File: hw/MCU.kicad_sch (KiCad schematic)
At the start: 15 parts, among them J2 Conn_01x06, SW2 SKRPACE010, SW3 SKRPACE010, U2 N32L406RBL7

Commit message: updated Sheet and Board Information
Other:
- company: Qingdao IotPi Information Technology Ltd., -> Beijing Exponential Deep Space
- title: KiCad 2023 Shen Zhen Badge -> KiCad 2023 Asia Badge
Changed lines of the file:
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@@
   (paper "A4")
   (title_block
-    (title "KiCad 2023 Shen Zhen Badge")
-    (date "2023-10-04")
+    (title "KiCad 2023 Asia Badge")
+    (date "2023-10-07")
     (rev "2")
-    (company "Qingdao IotPi Information Technology Ltd.,")
+    (company "Beijing Exponential Deep Space")
     (comment 1 "Designed by Yang Hongbo")
   )

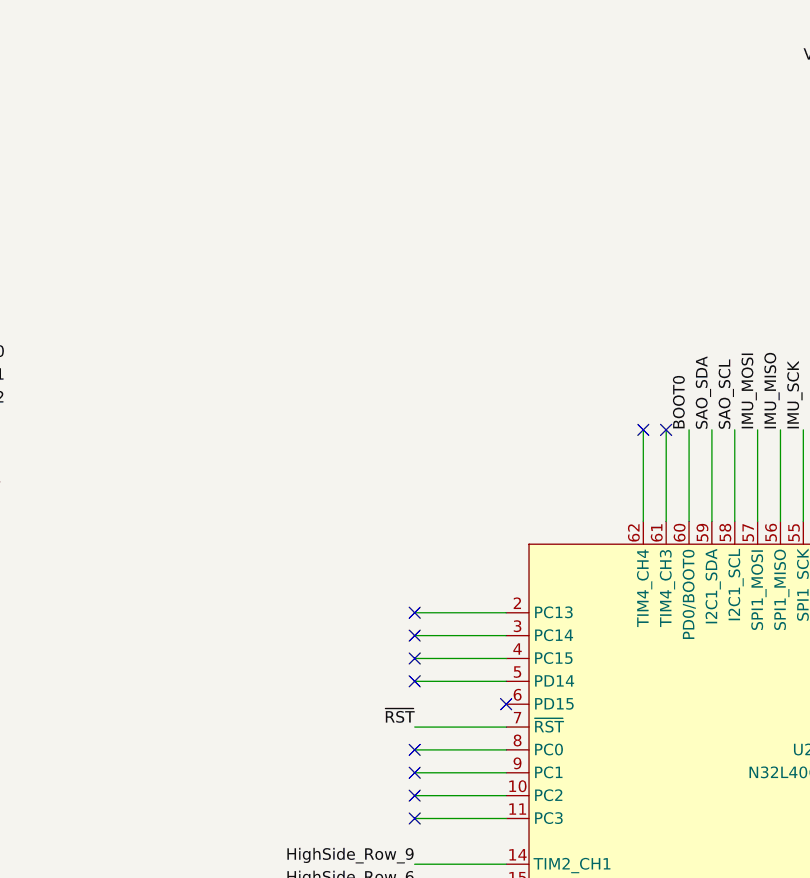
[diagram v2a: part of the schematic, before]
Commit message: added 8Mhz crystal
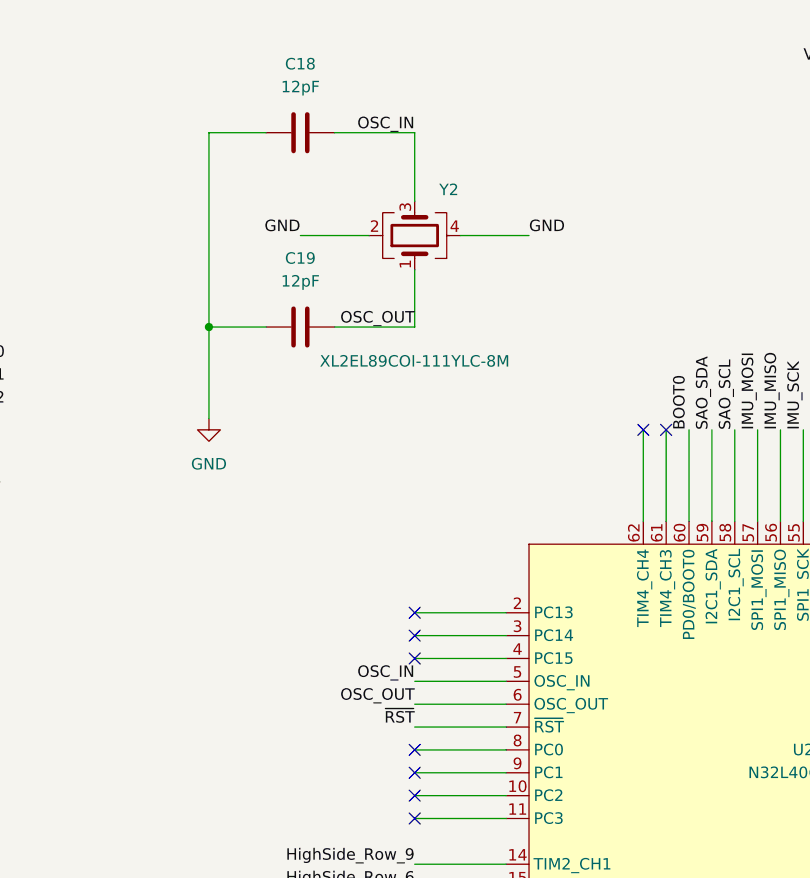
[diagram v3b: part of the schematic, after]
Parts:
- added C18, C19: 12pF, Capacitor_SMD:C_0402_1005Metric, symbol Device:C
- added Y2: XL2EL89COI-111YLC-8M, Crystal:Crystal_SMD_3225-4Pin_3.2x2.5mm, symbol Device:Crystal_GND24
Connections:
- net GND: now also C18.1, C19.1, Y2.2, Y2.4
- net OSC_IN: now reaches U2.5 (PD14)
- net OSC_IN: now also C18.2, Y2.3
- net OSC_OUT: now reaches U2.6 (PD15)
- net OSC_OUT: now also C19.2, Y2.1
- no-connect marks 18 -> 16
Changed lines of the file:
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@@
   (junction (at 114.3 172.72) (diameter 0) (color 0 0 0 0)
   )
+  (junction (at 91.44 49.53) (diameter 0) (color 0 0 0 0)
+  )
   (junction (at 264.16 142.24) (diameter 0) (color 0 0 0 0)
   )
@@
   (no_connect (at 209.55 137.16))
   (no_connect (at 114.3 96.52))
-  (no_connect (at 114.3 88.9))
   (no_connect (at 165.1 60.96))
   (no_connect (at 160.02 60.96))
   (no_connect (at 114.3 81.28))
-  (no_connect (at 124.46 91.44))
   (no_connect (at 114.3 104.14))
   (no_connect (at 114.3 83.82))
@@
     (stroke (width 0) (type default))
   )
+  (wire (pts (xy 114.3 27.94) (xy 114.3 35.56))
+    (stroke (width 0) (type default))
+  )
   (wire (pts (xy 209.55 147.32) (xy 209.55 137.16))
     (stroke (width 0) (type default))
@@
     (stroke (width 0) (type default))
   )
+  (wire (pts (xy 127 39.37) (xy 119.38 39.37))
+    (stroke (width 0) (type default))
+  )
+  (wire (pts (xy 97.79 27.94) (xy 91.44 27.94))
+    (stroke (width 0) (type default))
+  )
   (wire (pts (xy 190.5 104.14) (xy 200.66 104.14))
     (stroke (width 0) (type default))
@@
     (stroke (width 0) (type default))
   )
+  (wire (pts (xy 105.41 49.53) (xy 114.3 49.53))
+    (stroke (width 0) (type default))
+  )
   (wire (pts (xy 234.95 20.32) (xy 248.92 20.32))
     (stroke (width 0) (type default))
   )
+  (wire (pts (xy 124.46 91.44) (xy 114.3 91.44))
+    (stroke (width 0) (type default))
+  )
   (wire (pts (xy 181.61 30.48) (xy 181.61 33.02))
     (stroke (width 0) (type default))
@@
     (stroke (width 0) (type default))
   )
+  (wire (pts (xy 101.6 39.37) (xy 109.22 39.37))
+    (stroke (width 0) (type default))
+  )
   (wire (pts (xy 63.5 25.4) (xy 55.88 25.4))
     (stroke (width 0) (type default))
@@
     (stroke (width 0) (type default))
   )
+  (wire (pts (xy 91.44 49.53) (xy 91.44 59.69))
+    (stroke (width 0) (type default))
+  )
   (wire (pts (xy 168.91 33.02) (xy 162.56 33.02))
     (stroke (width 0) (type default))
@@
     (stroke (width 0) (type default))
   )
+  (wire (pts (xy 91.44 49.53) (xy 97.79 49.53))
+    (stroke (width 0) (type default))
+  )
+  (wire (pts (xy 91.44 27.94) (xy 91.44 49.53))
+    (stroke (width 0) (type default))
+  )
   (wire (pts (xy 142.24 127) (xy 142.24 137.16))
     (stroke (width 0) (type default))
@@
     (stroke (width 0) (type default))
   )
+  (wire (pts (xy 114.3 43.18) (xy 114.3 49.53))
+    (stroke (width 0) (type default))
+  )
   (wire (pts (xy 43.18 175.26) (xy 53.34 175.26))
     (stroke (width 0) (type default))
@@
     (stroke (width 0) (type default))
   )
+  (wire (pts (xy 105.41 27.94) (xy 114.3 27.94))
+    (stroke (width 0) (type default))
+  )
   (wire (pts (xy 147.32 127) (xy 147.32 137.16))
     (stroke (width 0) (type default))
@@
     (effects (font (size 1.27 1.27)) (justify left bottom))
   )
+  (label "GND" (at 101.6 39.37 180) (fields_autoplaced)
+    (effects (font (size 1.27 1.27)) (justify right bottom))
+  )
   (label "SAO_2_GPIO2" (at 200.66 91.44 0) (fields_autoplaced)
     (effects (font (size 1.27 1.27)) (justify left bottom))
@@
     (effects (font (size 1.27 1.27)) (justify right bottom))
   )
+  (label "OSC_IN" (at 114.3 27.94 180) (fields_autoplaced)
+    (effects (font (size 1.27 1.27)) (justify right bottom))
+  )
   (label "VDD" (at 207.01 137.16 90) (fields_autoplaced)
     (effects (font (size 1.27 1.27)) (justify left bottom))
@@
     (effects (font (size 1.27 1.27)) (justify right bottom))
   )
+  (label "OSC_IN" (at 114.3 88.9 180) (fields_autoplaced)
+    (effects (font (size 1.27 1.27)) (justify right bottom))
+  )
   (label "SAO_SCL" (at 53.34 124.46 0) (fields_autoplaced)
     (effects (font (size 1.27 1.27)) (justify left bottom))
   )
+  (label "GND" (at 127 39.37 0) (fields_autoplaced)
+    (effects (font (size 1.27 1.27)) (justify left bottom))
+  )
   (label "IMU_MOSI" (at 152.4 60.96 90) (fields_autoplaced)
     (effects (font (size 1.27 1.27)) (justify left bottom))
@@
     (effects (font (size 1.27 1.27)) (justify left bottom))
   )
+  (label "OSC_OUT" (at 114.3 91.44 180) (fields_autoplaced)
+    (effects (font (size 1.27 1.27)) (justify right bottom))
+  )
   (label "GND" (at 172.72 137.16 270) (fields_autoplaced)
     (effects (font (size 1.27 1.27)) (justify right bottom))
@@
     (effects (font (size 1.27 1.27)) (justify left bottom))
   )
+  (label "OSC_OUT" (at 114.3 49.53 180) (fields_autoplaced)
+    (effects (font (size 1.27 1.27)) (justify right bottom))
+  )
   (hierarchical_label "HighSide_Row_10" (shape output) (at 43.18 53.34 180) (fields_autoplaced)
     (effects (font (size 1.27 1.27)) (justify right))
@@
     )
   )
+  (symbol (lib_id "Device:C") (at 101.6 49.53 90) (unit 1)
+    (in_bom yes) (on_board yes) (dnp no) (fields_autoplaced)
+    (property "Reference" "C19" (at 101.6 41.91 90)
+      (effects (font (size 1.27 1.27)))
+    )
+    (property "Value" "12pF" (at 101.6 44.45 90)
+      (effects (font (size 1.27 1.27)))
+    )
+    (property "Footprint" "Capacitor_SMD:C_0402_1005Metric" (at 105.41 48.5648 0)
+      (effects (font (size 1.27 1.27)) hide)
+    )
+    (property "Datasheet" "~" (at 101.6 49.53 0)
+      (effects (font (size 1.27 1.27)) hide)
+    )
+    (property "Description" "容值：12pF 精度：±5% 额定电压：50V 材质(温度系数)：C0G 材质:C0G" (at 101.6 49.53 0)
+      (effects (font (size 1.27 1.27)) hide)
+    )
+    (property "LCSC" "C1547" (at 101.6 49.53 0)
+      (effects (font (size 1.27 1.27)) hide)
+    )
+    (property "Vendor" " FH(风华)" (at 101.6 49.53 0)
+      (effects (font (size 1.27 1.27)) hide)
+    )
+    (property "Vendor Model" "0402CG120J500NT" (at 101.6 49.53 0)
+      (effects (font (size 1.27 1.27)) hide)
+    )
+    (pin "1")
+    (pin "2")
+    (instances
+      (project "KiConSZ2023"
+        (path "/8659c260-f029-4e72-8b9a-85fff45eea40/aebeadc6-0cb2-44f8-88a5-80ae76b1b2bc"
+          (reference "C19") (unit 1)
+        )
+      )
+    )
+  )
   (symbol (lib_id "power:GND") (at 264.16 157.48 0) (unit 1)
     (in_bom yes) (on_board yes) (dnp no) (fields_autoplaced)
@@
     )
   )
+  (symbol (lib_id "Device:Crystal_GND24") (at 114.3 39.37 90) (unit 1)
+    (in_bom yes) (on_board yes) (dnp no)
+    (property "Reference" "Y2" (at 118.11 34.29 90)
+      (effects (font (size 1.27 1.27)))
+    )
+    (property "Value" "XL2EL89COI-111YLC-8M" (at 114.3 53.34 90)
+      (effects (font (size 1.27 1.27)))
+    )
+    (property "Footprint" "Crystal:Crystal_SMD_3225-4Pin_3.2x2.5mm" (at 114.3 39.37 0)
+      (effects (font (size 1.27 1.27)) hide)
+    )
+    (property "Datasheet" "~" (at 114.3 39.37 0)
+      (effects (font (size 1.27 1.27)) hide)
+    )
+    (property "Description" "无源晶振 YSX321SL 8MHZ 20PF ±10PPM" (at 114.3 39.37 0)
+      (effects (font (size 1.27 1.27)) hide)
+    )
+    (property "LCSC" "C2973805" (at 114.3 39.37 0)
+      (effects (font (size 1.27 1.27)) hide)
+    )
+    (property "Vendor" "YXC(扬兴晶振)" (at 114.3 39.37 0)
+      (effects (font (size 1.27 1.27)) hide)
+    )
+    (property "Vendor Model" "XL2EL89COI-111YLC-8M" (at 114.3 39.37 0)
+      (effects (font (size 1.27 1.27)) hide)
+    )
+    (pin "1")
+    (pin "2")
+    (pin "3")
+    (pin "4")
+    (instances
+      (project "KiConSZ2023"
+        (path "/8659c260-f029-4e72-8b9a-85fff45eea40/aebeadc6-0cb2-44f8-88a5-80ae76b1b2bc"
+          (reference "Y2") (unit 1)
+        )
+      )
+    )
+  )
   (symbol (lib_id "Device:C") (at 193.04 26.67 0) (unit 1)
     (in_bom yes) (on_board yes) (dnp no) (fields_autoplaced)
@@
     (pin "48")
     (pin "49" (alternate "SWCLK-JTCK"))
-    (pin "5")
+    (pin "5" (alternate "OSC_IN"))
     (pin "50" (alternate "SPI2_~{SS}"))
     (pin "51")
@@
     (pin "58" (alternate "I2C1_SCL"))
     (pin "59" (alternate "I2C1_SDA"))
-    (pin "6")
+    (pin "6" (alternate "OSC_OUT"))
     (pin "60")
     (pin "61" (alternate "TIM4_CH3"))
@@
         )
       )
+    )
+  )
+  (symbol (lib_id "Device:C") (at 101.6 27.94 90) (unit 1)
+    (in_bom yes) (on_board yes) (dnp no) (fields_autoplaced)
+    (property "Reference" "C18" (at 101.6 20.32 90)
+      (effects (font (size 1.27 1.27)))
+    )
+    (property "Value" "12pF" (at 101.6 22.86 90)
+      (effects (font (size 1.27 1.27)))
+    )
+    (property "Footprint" "Capacitor_SMD:C_0402_1005Metric" (at 105.41 26.9748 0)
+      (effects (font (size 1.27 1.27)) hide)
+    )
+    (property "Datasheet" "~" (at 101.6 27.94 0)
+      (effects (font (size 1.27 1.27)) hide)
+    )
+    (property "Description" "容值：12pF 精度：±5% 额定电压：50V 材质(温度系数)：C0G 材质:C0G" (at 101.6 27.94 0)
+      (effects (font (size 1.27 1.27)) hide)
+    )
+    (property "LCSC" "C1547" (at 101.6 27.94 0)
+      (effects (font (size 1.27 1.27)) hide)
+    )
+    (property "Vendor" " FH(风华)" (at 101.6 27.94 0)
+      (effects (font (size 1.27 1.27)) hide)
+    )
+    (property "Vendor Model" "0402CG120J500NT" (at 101.6 27.94 0)
+      (effects (font (size 1.27 1.27)) hide)
+    )
+    (pin "1")
+    (pin "2")
+    (instances
+      (project "KiConSZ2023"
+        (path "/8659c260-f029-4e72-8b9a-85fff45eea40/aebeadc6-0cb2-44f8-88a5-80ae76b1b2bc"
+          (reference "C18") (unit 1)
+        )
+      )
+    )
+  )
+  (symbol (lib_id "power:GND") (at 91.44 59.69 0) (unit 1)
+    (in_bom yes) (on_board yes) (dnp no) (fields_autoplaced)
+    (property "Reference" "#PWR09" (at 91.44 66.04 0)
+      (effects (font (size 1.27 1.27)) hide)
+    )
+    (property "Value" "GND" (at 91.44 64.77 0)
+      (effects (font (size 1.27 1.27)))
+    )
+    (property "Footprint" "" (at 91.44 59.69 0)
+      (effects (font (size 1.27 1.27)) hide)
+    )
+    (property "Datasheet" "" (at 91.44 59.69 0)
+      (effects (font (size 1.27 1.27)) hide)
+    )
+    (pin "1")
+    (instances
+      (project "KiConSZ2023"
+        (path "/8659c260-f029-4e72-8b9a-85fff45eea40/aebeadc6-0cb2-44f8-88a5-80ae76b1b2bc"
+          (reference "#PWR09") (unit 1)
+        )
+      )

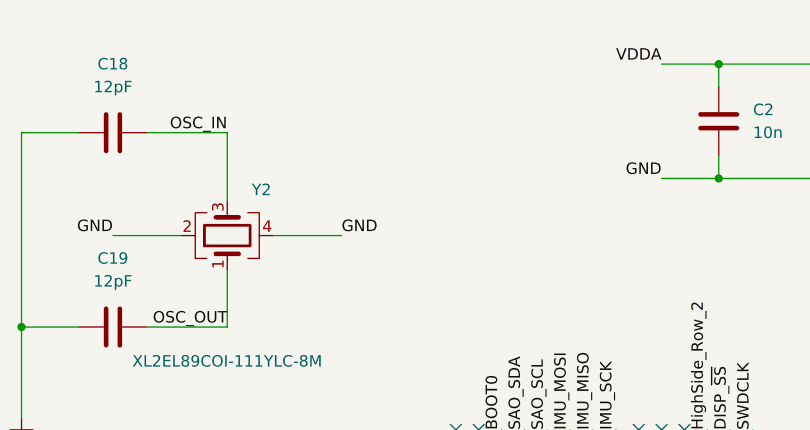
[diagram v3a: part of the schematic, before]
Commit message: added one comment for crystal
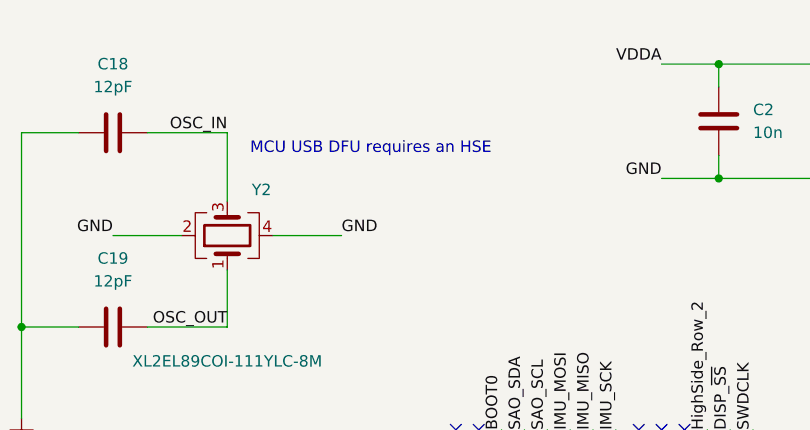
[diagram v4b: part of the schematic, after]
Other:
- note added: "MCU USB DFU requires an HSE"
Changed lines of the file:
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@@
+    (effects (font (size 1.27 1.27)) (justify left bottom))
+  )
+  (text "MCU USB DFU requires an HSE" (at 116.84 30.48 0)
     (effects (font (size 1.27 1.27)) (justify left bottom))
   )
